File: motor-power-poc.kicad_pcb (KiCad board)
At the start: 4 copper layers, 70 x 50 mm, 158 parts, among them J1 Conn_01x04_Pin, J2 USB_C_Receptacle_USB2.0_14P, J3 Conn_01x02, J4 Conn_02x02_Counter_Clockwise, J5 Conn_02x06_Counter_Clockwise, M1 Motor_Servo, M2 Motor_Servo, M3 DC, Q1 Q_NMOS, Q10 Q_NMOS, Q2 Q_NMOS, Q3 Q_NMOS, Q4 Q_NMOS, Q5 Q_NMOS, Q6 Q_NMOS, Q7 Q_NMOS, Q8 Q_NMOS, Q9 Q_NMOS, SW1 SW_Push, SW2 SW_Push, U1 QRE1113GR, U10 CJ431, U11 DRV8701, U2 QRE1113GR, U3 QRE1113GR, U4 ESP32-S3FH4R2, U5 LM74502, U6 TPS5430DDA, U7 TPS56A37, U8 TPS2121, U9 LDL212PV33R, Y1 48M

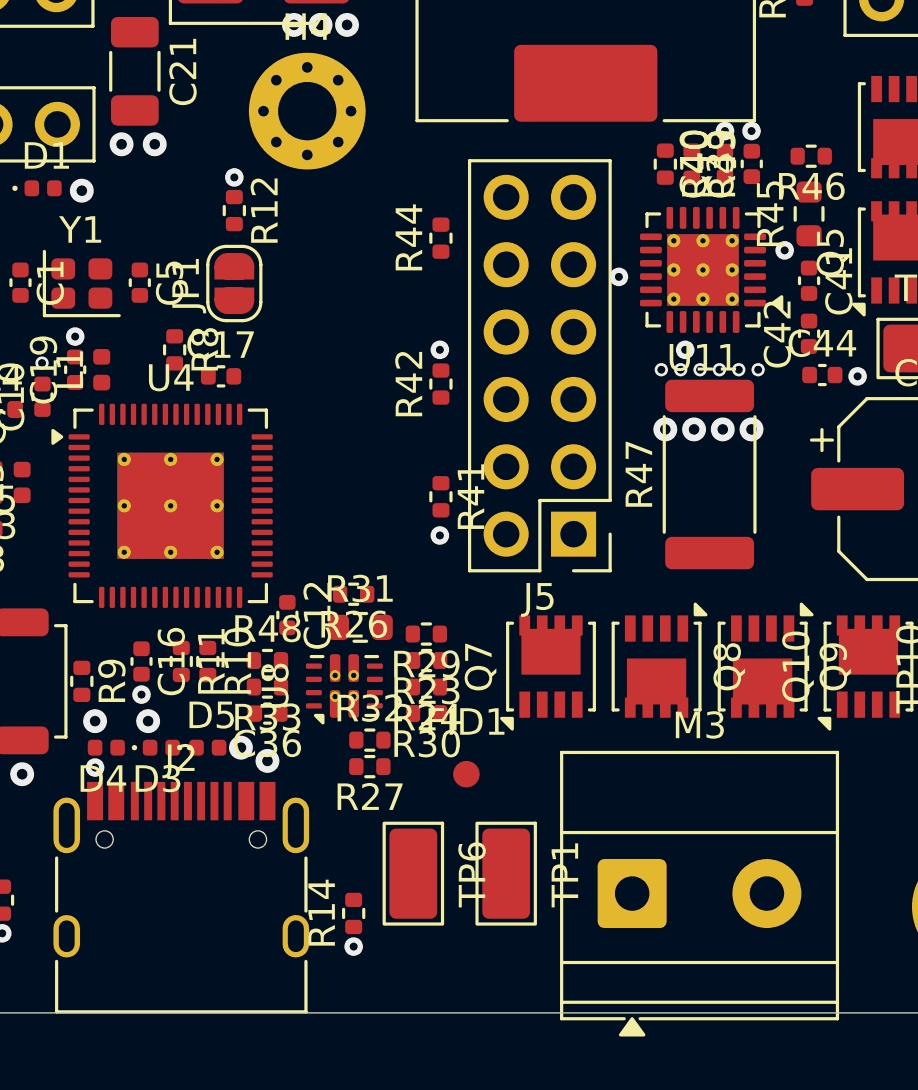
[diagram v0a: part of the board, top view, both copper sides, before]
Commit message: schem: ESP32 pin reorganisation
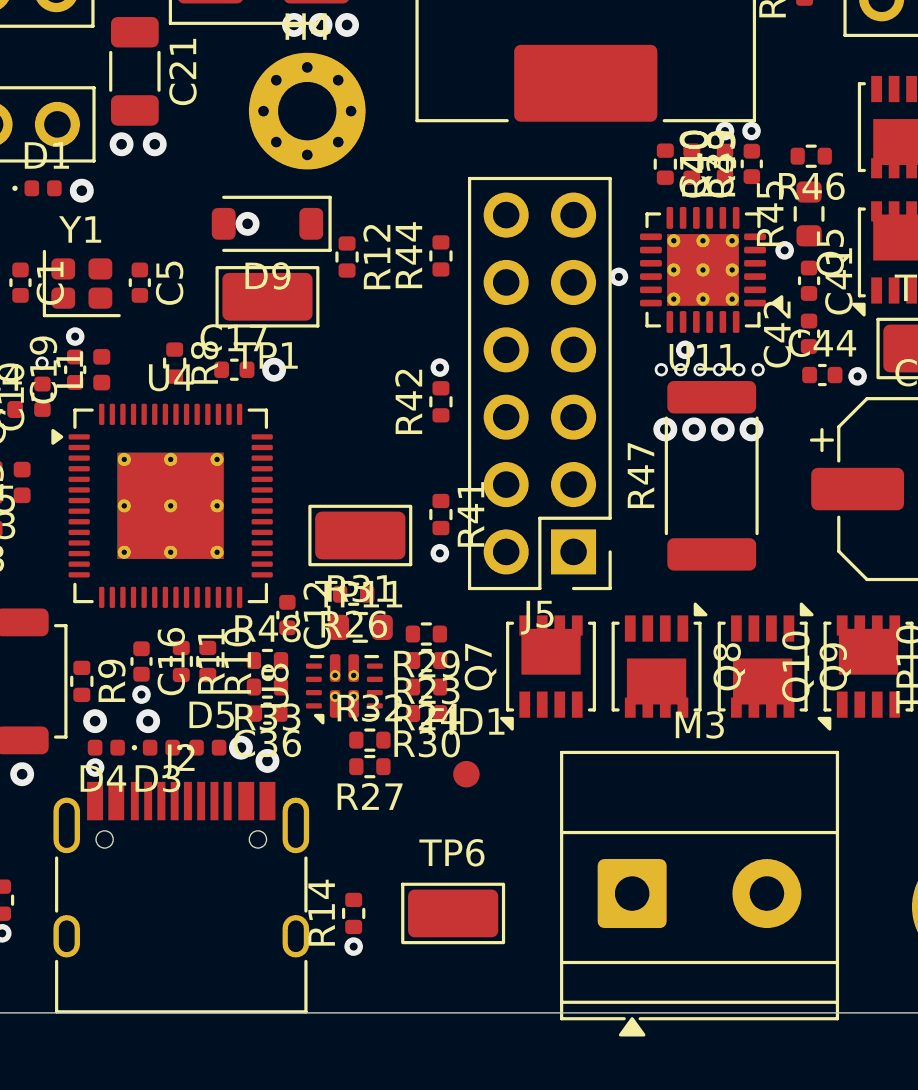
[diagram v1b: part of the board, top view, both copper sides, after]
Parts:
- removed JP1: Jumper_2_Open, Jumper:SolderJumper-2_P1.3mm_Open_RoundedPad1.0x1.5mm
- added D9: BZT52B3V3, Diode_SMD:D_SOD-123, F.Cu at (137.5, 74.2)
- added TP11: TestPoint, GLCS:TestPoint_Keystone_5015_Micro_Mini, F.Cu at (141.0, 86.0)
- moved TP1 23.5 mm to (137.5, 77.0), turned to 180 degrees
- moved R12 4.60 mm to (140.5, 75.5)
- moved TP6 2.12 mm to (144.5, 100.2), turned to 0 degrees
- moved J5 0.67 mm to (149.0, 86.6)
- moved R41 0.67 mm to (144.0, 85.2)
- moved R42 0.67 mm to (144.0, 81.0)
- moved R44 0.67 mm to (144.0, 75.5)
- moved C17 0.56 mm to (136.2, 79.8)
- moved R8 0.50 mm to (134.0, 79.5)
- moved R47 0.09 mm to (154.2, 83.8)
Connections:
- R12 pad 1: GND -> Net-(D9-K)
- R12 pad 2: Net-(JP1-B) -> SO
- U4 pad 10: PH -> unconnected-(U4-GPIO5/ADC1_CH4-Pad10)
- U4 pad 11: EN -> unconnected-(U4-GPIO6/ADC1_CH5-Pad11)
- U4 pad 13: /LS1 -> /LS3
- U4 pad 15: /LS3 -> /LS1
- U4 pad 36: SO -> Net-(D9-K)
- U4 pad 38: SNSOUT -> unconnected-(U4-GPIO33-Pad38)
- U4 pad 39: SERVO2 -> PH
- U4 pad 40: SERVO1 -> EN
- U4 pad 42: ~{FAULT} -> SNSOUT
- U4 pad 43: unconnected-(U4-GPIO38-Pad43) -> ~{FAULT}
- U4 pad 47: unconnected-(U4-MTDI/JTAG/GPIO41-Pad47) -> SERVO1
- U4 pad 48: unconnected-(U4-MTMS/JTAG/GPIO42-Pad48) -> SERVO2
- U4 pad 52: Net-(JP1-A) -> unconnected-(U4-GPIO46-Pad52)
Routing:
- net GND: vias 92 -> 93

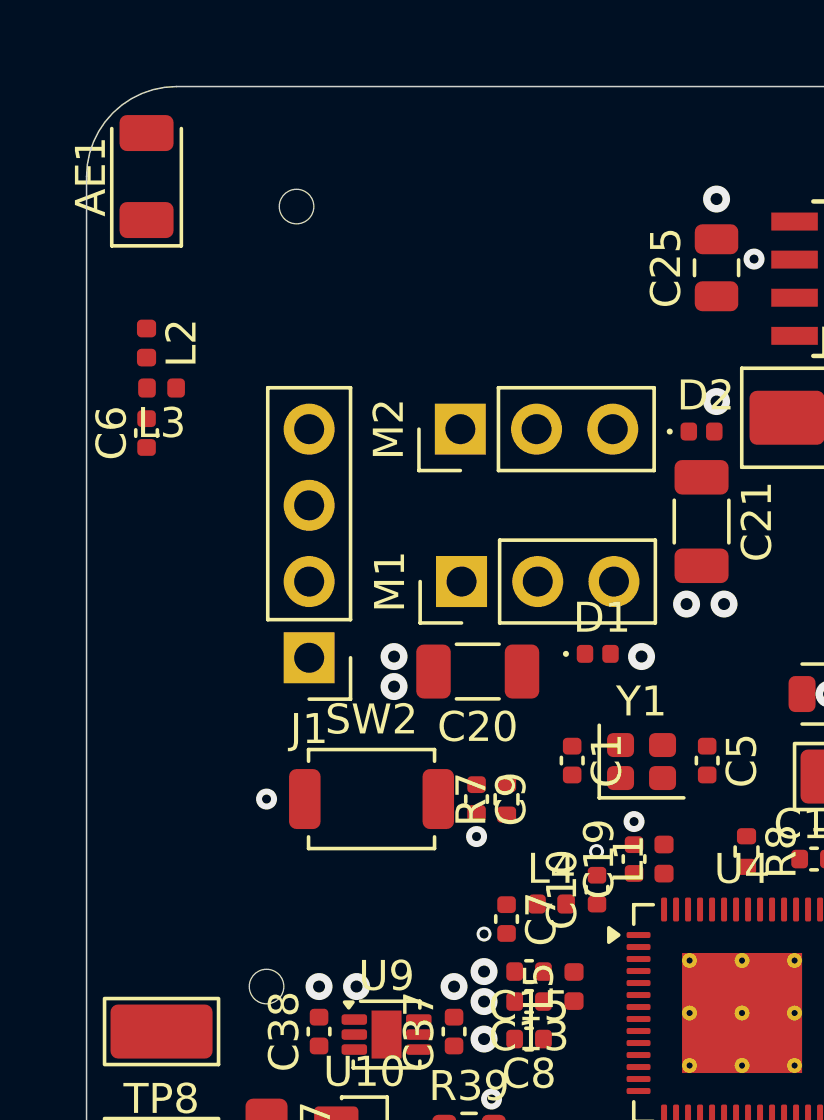
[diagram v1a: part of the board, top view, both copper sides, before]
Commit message: pcb: add rf routing
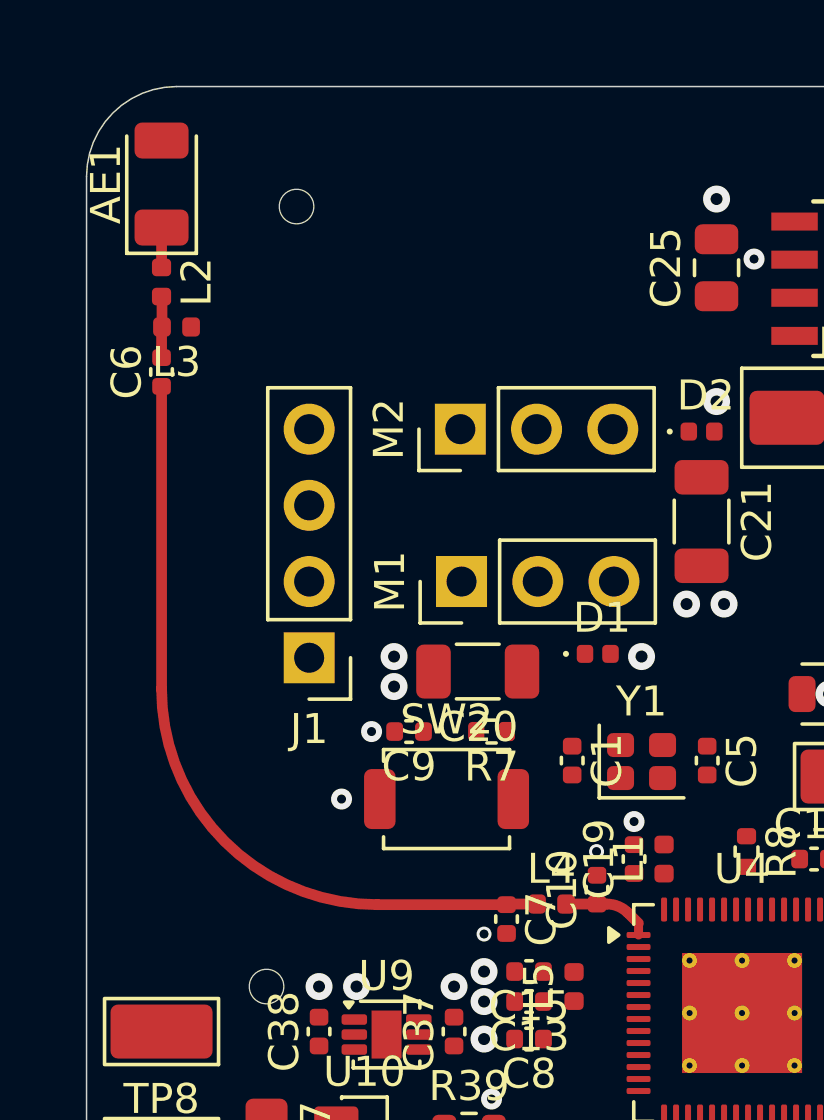
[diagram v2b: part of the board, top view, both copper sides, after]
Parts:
- moved C9 3.18 mm to (122.8, 75.5), turned to 180 degrees
- moved SW2 2.50 mm to (124.0, 77.8)
- moved R7 2.31 mm to (125.5, 75.5), turned to 180 degrees
- moved C6 2.10 mm to (114.5, 63.5)
- moved L2 2.10 mm to (114.5, 60.5)
- moved L3 2.10 mm to (115.0, 62.0)
- moved AE1 0.56 mm to (114.5, 57.2)
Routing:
- net /RF_TRANS: track 0.00 -> 26.4 mm
- net /RF_ESP: track 0.00 -> 2.91 mm
- net Net-(C6-Pad2): track 0.00 -> 2.05 mm
- net /RF_ANT: track 0.00 -> 1.33 mm

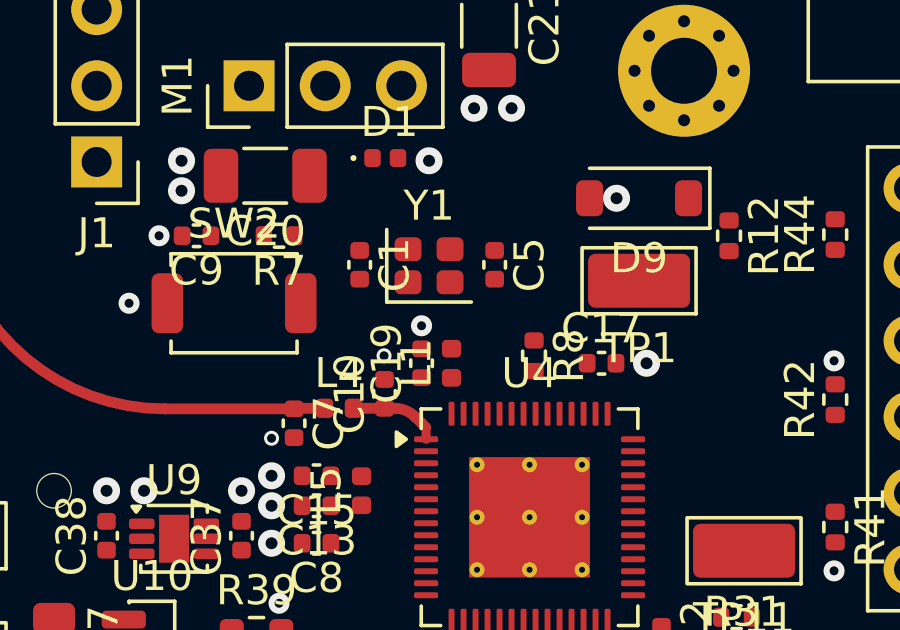
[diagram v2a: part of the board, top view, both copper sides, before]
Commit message: pcb: add crystal routing
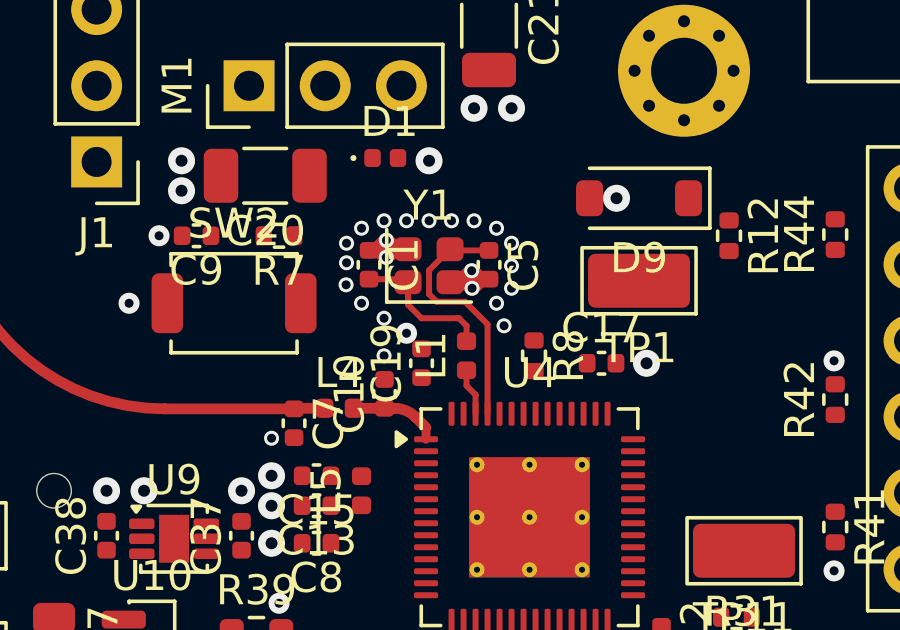
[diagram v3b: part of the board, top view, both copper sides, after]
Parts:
- moved L1 0.56 mm to (131.8, 79.5)
- moved C1 0.31 mm to (128.5, 76.5)
- moved C5 0.19 mm to (132.5, 76.5)
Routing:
- net /XTAL_N: track 0.00 -> 8.45 mm
- net GND: track 0.00 -> 6.16 mm, vias 93 -> 114
- net /XTAL_PL: track 0.00 -> 4.85 mm
- net /XTAL_P: track 0.00 -> 1.57 mm

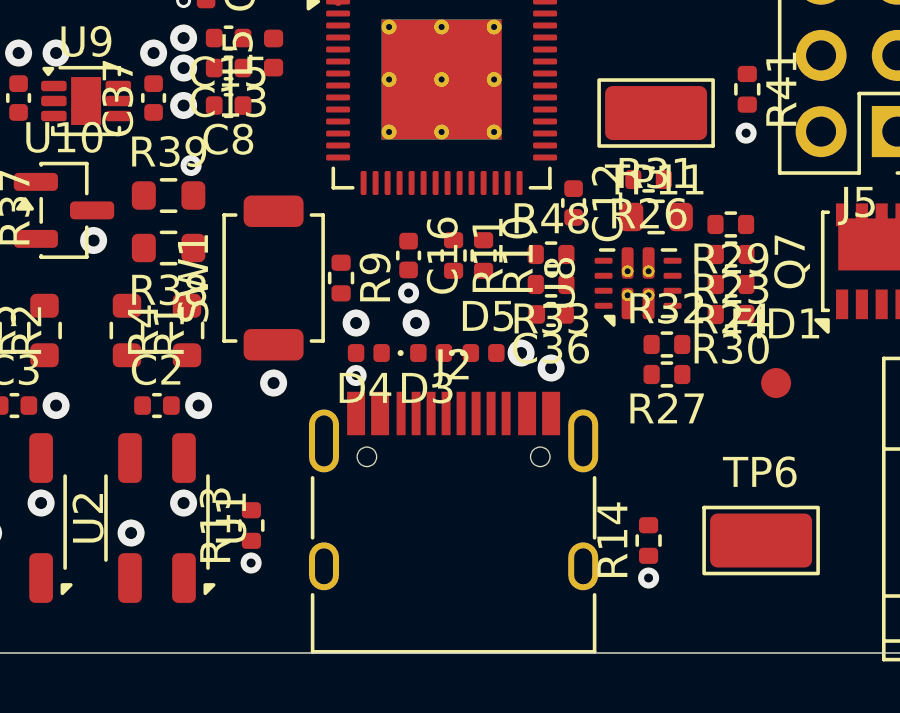
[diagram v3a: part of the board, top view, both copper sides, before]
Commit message: pcb: add USB routing
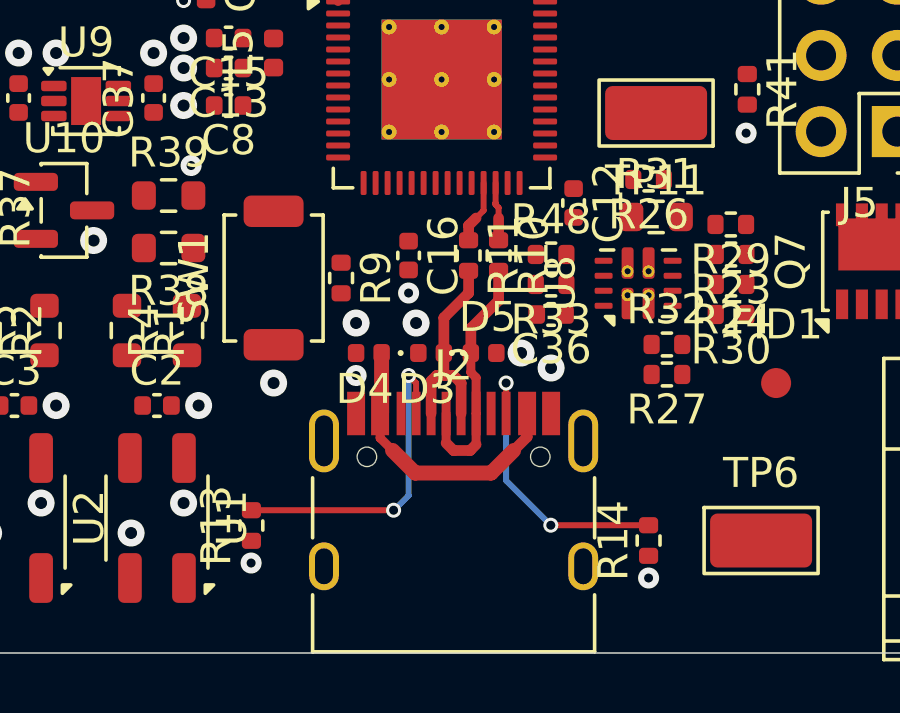
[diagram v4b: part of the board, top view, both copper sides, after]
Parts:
- moved R10 0.50 mm to (135.8, 90.8)
- moved R11 0.50 mm to (134.8, 90.8)
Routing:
- net Net-(J2-CC1): track 0.00 -> 10.8 mm, vias 0 -> 2
- net Net-(J2-CC2): track 0.00 -> 9.63 mm, vias 0 -> 2
- net +Vbus: track 0.00 -> 9.52 mm
- net D+: track 0.00 -> 8.42 mm
- net D-: track 0.00 -> 7.14 mm
- net /ESP_D-: track 0.00 -> 2.11 mm
- net /ESP_D+: track 0.00 -> 1.95 mm

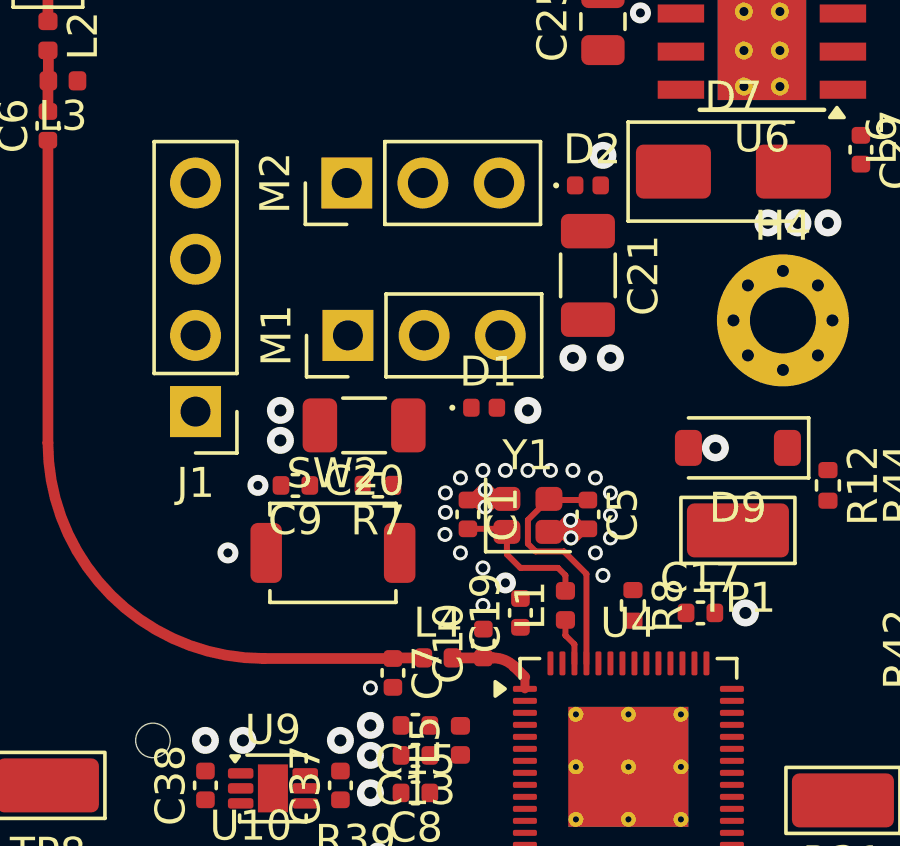
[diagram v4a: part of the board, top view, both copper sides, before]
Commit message: pcb: add UART and servo PWM routing
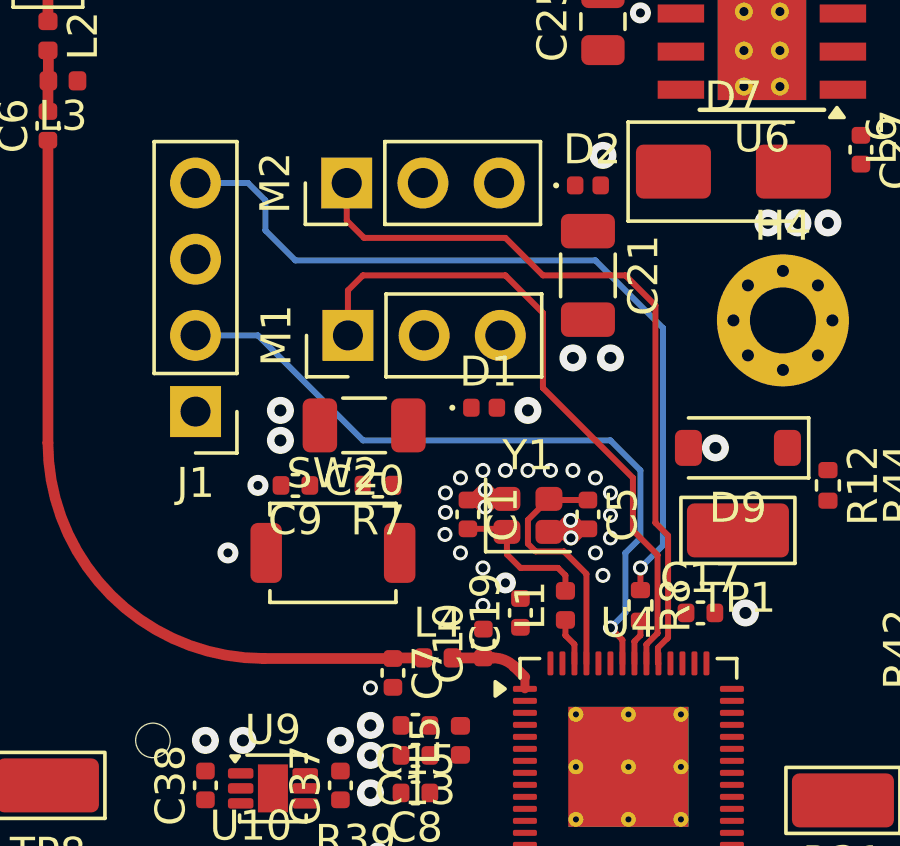
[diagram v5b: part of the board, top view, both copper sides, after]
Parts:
- moved R8 0.25 mm to (134.2, 79.5)
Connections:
- U4 pad 47: SERVO1 -> SERVO2
- U4 pad 48: SERVO2 -> SERVO1
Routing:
- net Net-(J1-Pin_4): track 0.00 -> 27.2 mm, vias 0 -> 1
- net SERVO2: track 0.00 -> 25.0 mm
- net /U0RXD: track 0.00 -> 23.7 mm, vias 0 -> 1
- net SERVO1: track 0.00 -> 22.1 mm
- net /U0TXD: track 0.00 -> 1.51 mm

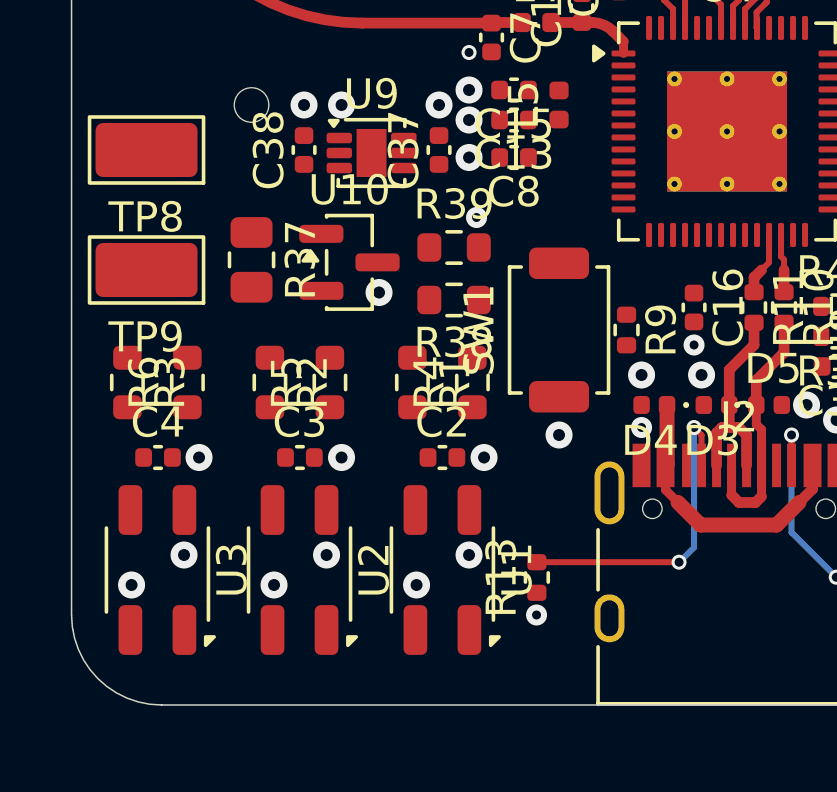
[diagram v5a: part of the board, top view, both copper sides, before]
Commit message: pcb: add QR1113 routing
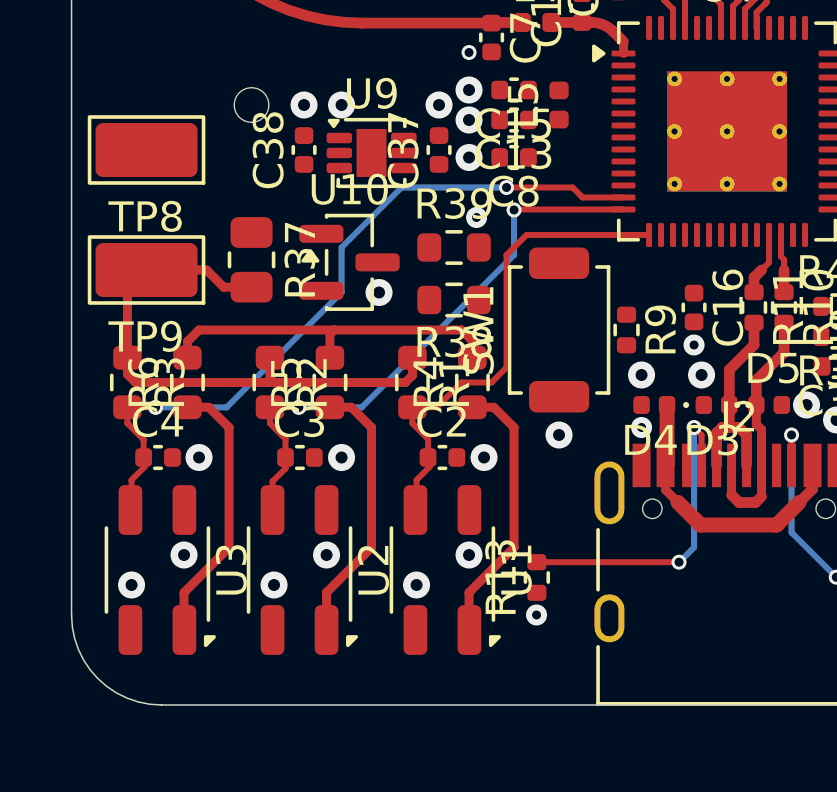
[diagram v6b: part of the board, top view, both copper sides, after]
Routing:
- net /LS3: track 0.00 -> 24.4 mm, vias 0 -> 2
- net /LS2: track 0.00 -> 19.2 mm, vias 0 -> 2
- net +3V: track 0.00 -> 18.7 mm
- net /LS1: track 0.00 -> 16.3 mm
- net +3V3: track 0.00 -> 11.9 mm
- net Net-(U3-A): track 0.00 -> 9.04 mm
- net Net-(U2-A): track 0.00 -> 9.04 mm
- net Net-(U1-A): track 0.00 -> 9.04 mm
